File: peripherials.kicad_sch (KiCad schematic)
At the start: 58 parts, among them J11 JST_SH_1x2_SM02B-SRSS-TB-LF-SN, U15 PN7160AHN

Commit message: [#54617] Update bus naming; remove DNP for TVS
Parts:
- D? (x10): DNP DNP -> (none)
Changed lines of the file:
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@@
       (effects (font (size 1.27 1.27) (thickness 0.15)) (justify left bottom) hide)
-    )
-    (property "DNP" "DNP" (at 146.05 213.3599 0)
-      (effects (font (size 1.27 1.27)) (justify left) hide)
     )
     (pin "1")
@@
       (effects (font (size 1.27 1.27) (thickness 0.15)) (justify left bottom) hide)
     )
-    (property "DNP" "DNP" (at 196.85 194.3099 0)
-      (effects (font (size 1.27 1.27)) (justify left) hide)
-    )
     (pin "1")
     (pin "10")
@@
       (effects (font (size 1.27 1.27) (thickness 0.15)) (justify left bottom) hide)
     )
-    (property "DNP" "DNP" (at 146.05 193.0399 0)
-      (effects (font (size 1.27 1.27)) (justify left) hide)
-    )
     (pin "1")
     (pin "10")
@@
       (effects (font (size 1.27 1.27) (thickness 0.15)) (justify left bottom) hide)
     )
-    (property "DNP" "DNP" (at 146.05 173.9899 0)
-      (effects (font (size 1.27 1.27)) (justify left) hide)
-    )
     (pin "1")
     (pin "10")
@@
       (effects (font (size 1.27 1.27) (thickness 0.15)) (justify left bottom) hide)
     )
-    (property "DNP" "DNP" (at 196.85 175.2599 0)
-      (effects (font (size 1.27 1.27)) (justify left) hide)
-    )
     (pin "1")
     (pin "10")
@@
       (effects (font (size 1.27 1.27) (thickness 0.15)) (justify left bottom) hide)
     )
-    (property "DNP" "DNP" (at 196.85 233.6799 0)
-      (effects (font (size 1.27 1.27)) (justify left) hide)
-    )
     (pin "1")
     (pin "10")
@@
     (property "License" "Apache-2.0" (at 157.48 245.11 0)
       (effects (font (size 1.27 1.27) (thickness 0.15)) (justify left bottom) hide)
-    )
-    (property "DNP" "DNP" (at 146.05 232.4099 0)
-      (effects (font (size 1.27 1.27)) (justify left) hide)
     )
     (pin "1")
@@
       (effects (font (size 1.27 1.27) (thickness 0.15)) (justify left bottom) hide)
     )
-    (property "DNP" "DNP" (at 196.85 214.6299 0)
-      (effects (font (size 1.27 1.27)) (justify left) hide)
-    )
     (pin "1")
     (pin "10")
@@
       (effects (font (size 1.27 1.27) (thickness 0.15)) (justify left bottom) hide)
     )
-    (property "DNP" "DNP" (at 135.89 109.2199 0)
-      (effects (font (size 1.27 1.27)) (justify left) hide)
-    )
     (pin "1")
     (pin "10")
@@
       (effects (font (size 1.27 1.27) (thickness 0.15)) (justify left bottom) hide)
     )
-    (property "DNP" "DNP" (at 134.62 46.9899 0)
-      (effects (font (size 1.27 1.27)) (justify left) hide)
-    )
-    (pin "1")
+    (pin "1")

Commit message: [#54617] Review requested changes
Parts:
- L? (x2): footprint antmicro-footprints:L_0603_1608Metric -> antmicro-footprints:

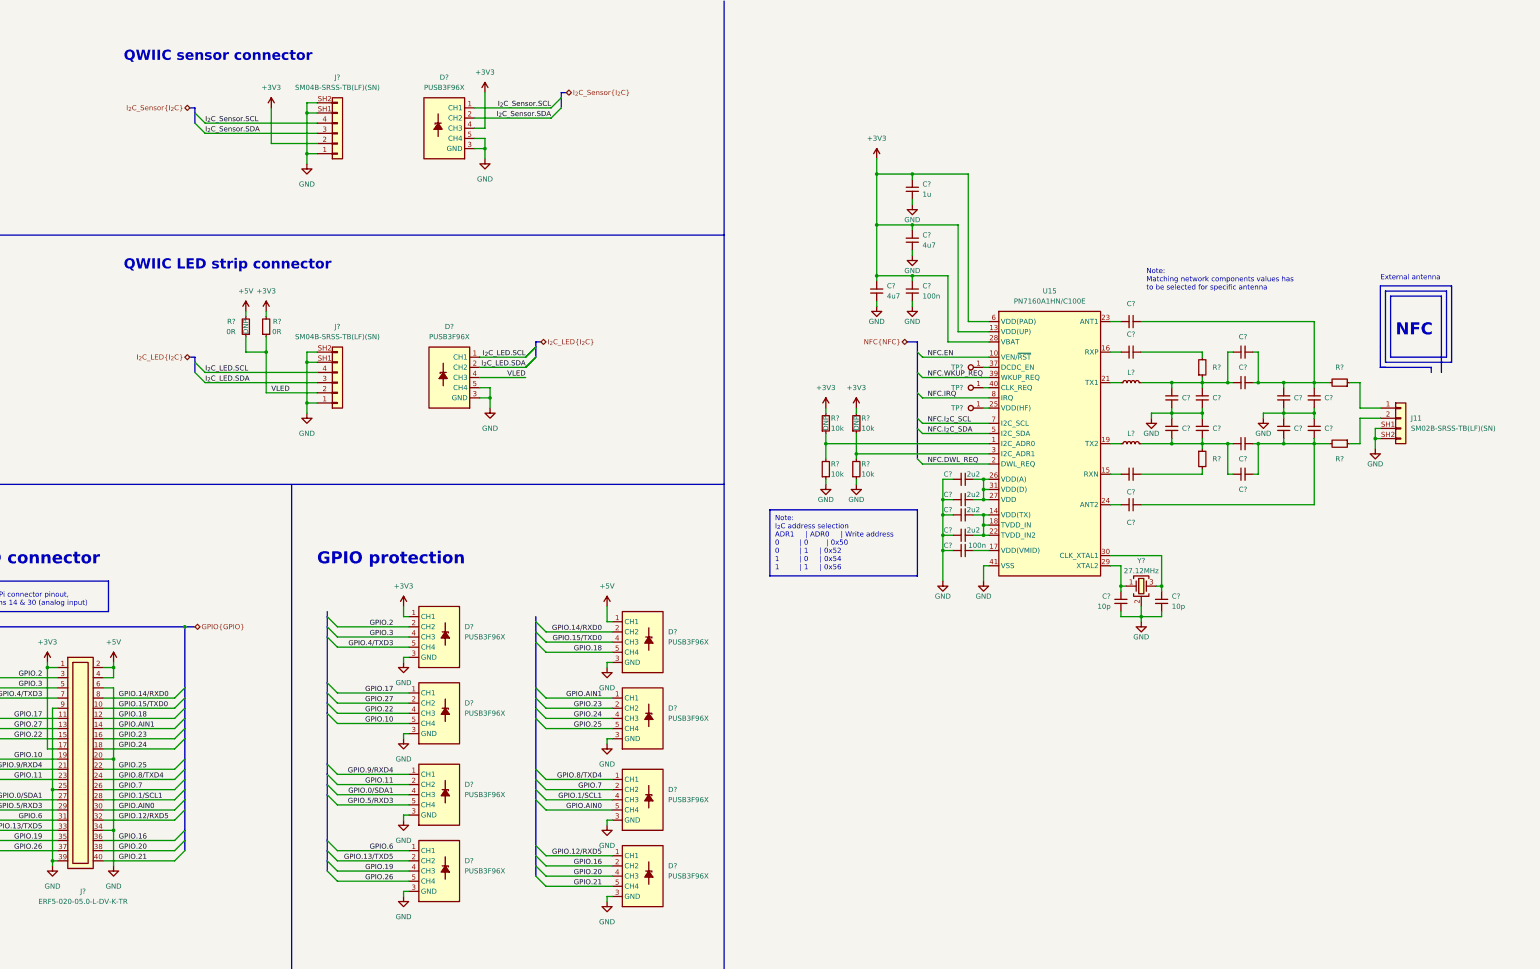
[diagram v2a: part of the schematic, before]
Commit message: [#54617] Re-enumerate reference designators
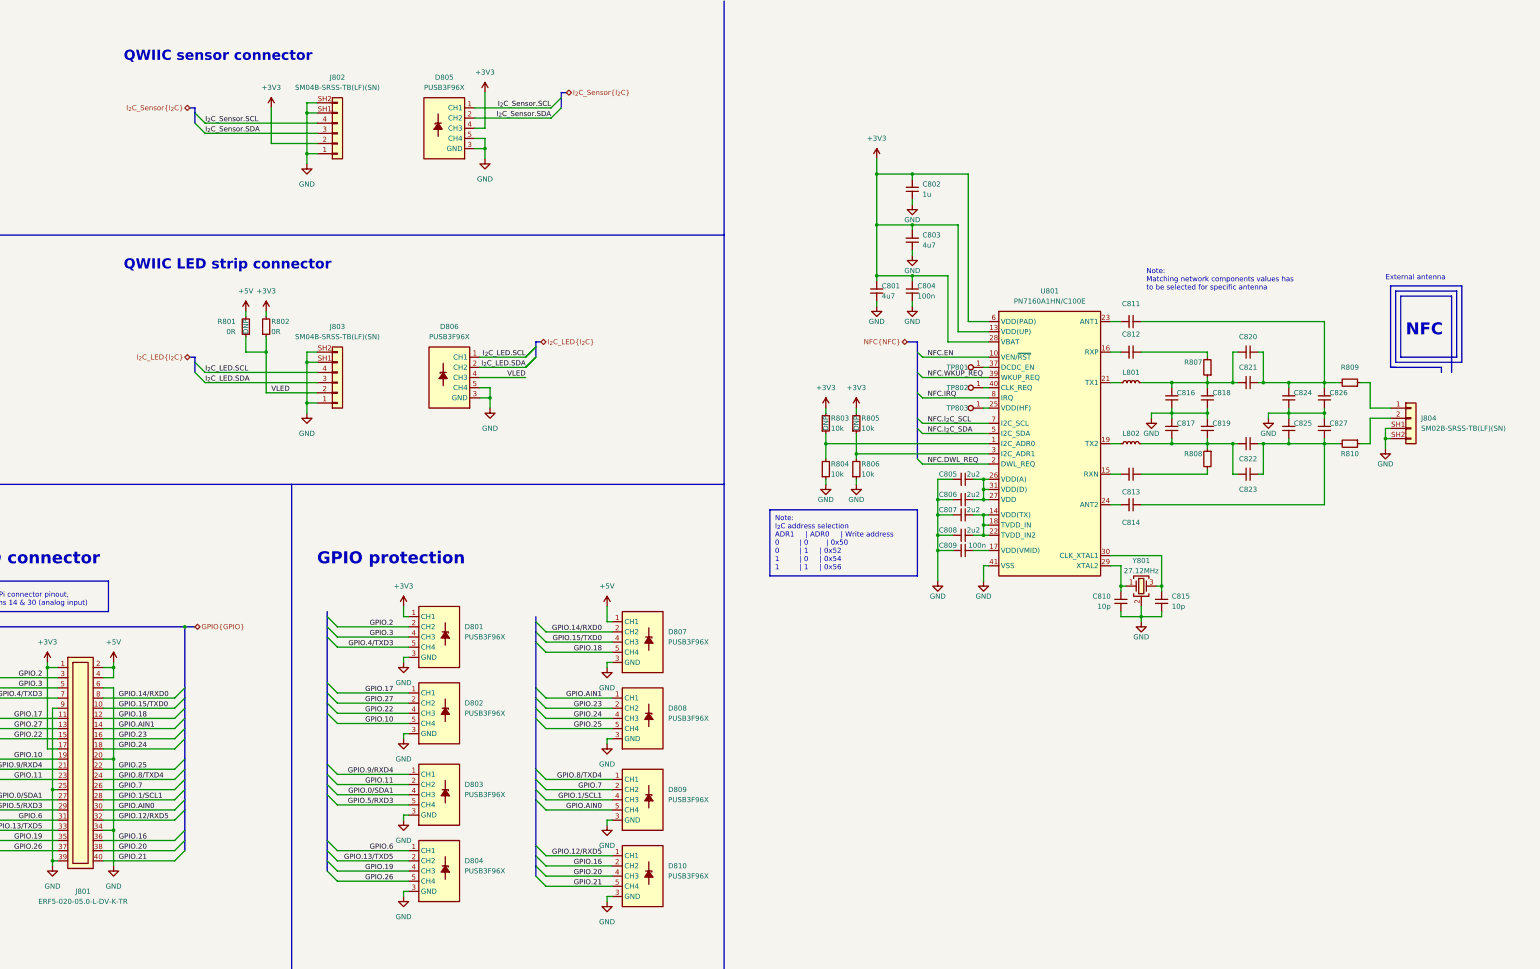
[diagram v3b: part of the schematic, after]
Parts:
- gave numbers to parts that had none: 56
- renumbered J11 to J804, U15 to U801
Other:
- moved on the sheet: C818, C819, C820, C821, C822, C823, C824, C825, C826, C827, J804, R807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

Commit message: [#55181] Rotate board; Change CSI&SD position; Update adapter; NFC placement
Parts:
- L801, L802: footprint antmicro-footprints: -> antmicro-footprints:L_0603_1608Metric
- TP801, TP802, TP803: footprint antmicro-footprints:TP_SMD_1mm -> antmicro-footprints:TP_SMD_0.75mm; symbol antmicroTestPoints:TP_1mm_SMD -> antmicroTestPoints:TP_0.75mm_SMD; now left out of the parts list
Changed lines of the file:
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@@
     )
   )
-  (symbol (lib_id "antmicroTestPoints:TP_1mm_SMD") (at 275.59 114.3 180) (unit 1)
-    (in_bom yes) (on_board yes) (dnp no)
+  (symbol (lib_id "antmicroTestPoints:TP_0.75mm_SMD") (at 275.59 114.3 180) (unit 1)
+    (in_bom no) (on_board yes) (dnp no)
     (property "Reference" "TP803" (at 271.78 114.3 0)
       (effects (font (size 1.27 1.27) (thickness 0.15)) (justify left))
@@
       (effects (font (size 1.27 1.27) (thickness 0.15)) (justify left bottom) hide)
     )
-    (property "Footprint" "antmicro-footprints:TP_SMD_1mm" (at 260.35 104.14 0)
-      (effects (font (size 1.27 1.27) (thickness 0.15)) (justify left bottom) hide)
-    )
-    (property "Datasheet" "" (at 260.35 101.6 0)
-      (effects (font (size 1.27 1.27) (thickness 0.15)) (justify left bottom) hide)
-    )
-    (property "Author" "Antmicro" (at 260.35 99.06 0)
-      (effects (font (size 1.27 1.27) (thickness 0.15)) (justify left bottom) hide)
-    )
-    (property "License" "Apache-2.0" (at 260.35 96.52 0)
-      (effects (font (size 1.27 1.27) (thickness 0.15)) (justify left bottom) hide)
-    )
-    (property "MPN" "" (at 275.59 114.3 0)
-      (effects (font (size 1.27 1.27)) hide)
-    )
-    (property "Manufacturer" "" (at 275.59 114.3 0)
-      (effects (font (size 1.27 1.27)) hide)
+    (property "Footprint" "antmicro-footprints:TP_SMD_0.75mm" (at 264.795 107.95 0)
+      (effects (font (size 1.27 1.27) (thickness 0.15)) (justify left bottom) hide)
+    )
+    (property "Datasheet" "" (at 257.81 101.6 0)
+      (effects (font (size 1.27 1.27) (thickness 0.15)) (justify left bottom) hide)
+    )
+    (property "Author" "Antmicro" (at 264.795 105.41 0)
+      (effects (font (size 1.27 1.27) (thickness 0.15)) (justify left bottom) hide)
+    )
+    (property "License" "Apache-2.0" (at 264.795 102.87 0)
+      (effects (font (size 1.27 1.27) (thickness 0.15)) (justify left bottom) hide)
+    )
+    (property "MPN" "" (at 264.795 102.87 0)
+      (effects (font (size 1.27 1.27) (thickness 0.15)) (justify left bottom) hide)
+    )
+    (property "Manufacturer" "" (at 264.795 107.95 0)
+      (effects (font (size 1.27 1.27) (thickness 0.15)) (justify left bottom) hide)
     )
     (pin "1")
@@
     )
   )
-  (symbol (lib_id "antmicroTestPoints:TP_1mm_SMD") (at 275.59 104.14 180) (unit 1)
-    (in_bom yes) (on_board yes) (dnp no)
+  (symbol (lib_id "antmicroTestPoints:TP_0.75mm_SMD") (at 275.59 104.14 180) (unit 1)
+    (in_bom no) (on_board yes) (dnp no)
     (property "Reference" "TP801" (at 271.78 104.14 0)
       (effects (font (size 1.27 1.27) (thickness 0.15)) (justify left))
@@
       (effects (font (size 1.27 1.27) (thickness 0.15)) (justify left bottom) hide)
     )
-    (property "Footprint" "antmicro-footprints:TP_SMD_1mm" (at 260.35 93.98 0)
-      (effects (font (size 1.27 1.27) (thickness 0.15)) (justify left bottom) hide)
-    )
-    (property "Datasheet" "" (at 260.35 91.44 0)
-      (effects (font (size 1.27 1.27) (thickness 0.15)) (justify left bottom) hide)
-    )
-    (property "Author" "Antmicro" (at 260.35 88.9 0)
-      (effects (font (size 1.27 1.27) (thickness 0.15)) (justify left bottom) hide)
-    )
-    (property "License" "Apache-2.0" (at 260.35 86.36 0)
-      (effects (font (size 1.27 1.27) (thickness 0.15)) (justify left bottom) hide)
-    )
-    (property "MPN" "" (at 275.59 104.14 0)
-      (effects (font (size 1.27 1.27)) hide)
-    )
-    (property "Manufacturer" "" (at 275.59 104.14 0)
-      (effects (font (size 1.27 1.27)) hide)
+    (property "Footprint" "antmicro-footprints:TP_SMD_0.75mm" (at 264.795 97.79 0)
+      (effects (font (size 1.27 1.27) (thickness 0.15)) (justify left bottom) hide)
+    )
+    (property "Datasheet" "" (at 257.81 91.44 0)
+      (effects (font (size 1.27 1.27) (thickness 0.15)) (justify left bottom) hide)
+    )
+    (property "Author" "Antmicro" (at 264.795 95.25 0)
+      (effects (font (size 1.27 1.27) (thickness 0.15)) (justify left bottom) hide)
+    )
+    (property "License" "Apache-2.0" (at 264.795 92.71 0)
+      (effects (font (size 1.27 1.27) (thickness 0.15)) (justify left bottom) hide)
+    )
+    (property "MPN" "" (at 264.795 92.71 0)
+      (effects (font (size 1.27 1.27) (thickness 0.15)) (justify left bottom) hide)
+    )
+    (property "Manufacturer" "" (at 264.795 97.79 0)
+      (effects (font (size 1.27 1.27) (thickness 0.15)) (justify left bottom) hide)
     )
     (pin "1")
@@
       (effects (font (size 1.27 1.27) (thickness 0.15)) (justify left bottom) hide)
     )
-    (property "Footprint" "antmicro-footprints:" (at 323.85 130.81 0)
+    (property "Footprint" "antmicro-footprints:L_0603_1608Metric" (at 323.85 130.81 0)
       (effects (font (size 1.27 1.27) (thickness 0.15)) (justify left bottom) hide)
     )
@@
       (effects (font (size 1.27 1.27) (thickness 0.15)) (justify left bottom) hide)
     )
-    (property "Footprint" "antmicro-footprints:" (at 323.85 115.57 0)
+    (property "Footprint" "antmicro-footprints:L_0603_1608Metric" (at 323.85 115.57 0)
       (effects (font (size 1.27 1.27) (thickness 0.15)) (justify left bottom) hide)
     )
@@
     )
   )
-  (symbol (lib_id "antmicroTestPoints:TP_1mm_SMD") (at 275.59 109.22 180) (unit 1)
-    (in_bom yes) (on_board yes) (dnp no)
+  (symbol (lib_id "antmicroTestPoints:TP_0.75mm_SMD") (at 275.59 109.22 180) (unit 1)
+    (in_bom no) (on_board yes) (dnp no)
     (property "Reference" "TP802" (at 271.78 109.22 0)
       (effects (font (size 1.27 1.27) (thickness 0.15)) (justify left))
@@
       (effects (font (size 1.27 1.27) (thickness 0.15)) (justify left bottom) hide)
     )
-    (property "Footprint" "antmicro-footprints:TP_SMD_1mm" (at 260.35 99.06 0)
-      (effects (font (size 1.27 1.27) (thickness 0.15)) (justify left bottom) hide)
-    )
-    (property "Datasheet" "" (at 260.35 96.52 0)
-      (effects (font (size 1.27 1.27) (thickness 0.15)) (justify left bottom) hide)
-    )
-    (property "Author" "Antmicro" (at 260.35 93.98 0)
-      (effects (font (size 1.27 1.27) (thickness 0.15)) (justify left bottom) hide)
-    )
-    (property "License" "Apache-2.0" (at 260.35 91.44 0)
-      (effects (font (size 1.27 1.27) (thickness 0.15)) (justify left bottom) hide)
-    )
-    (property "MPN" "" (at 275.59 109.22 0)
-      (effects (font (size 1.27 1.27)) hide)
-    )
-    (property "Manufacturer" "" (at 275.59 109.22 0)
-      (effects (font (size 1.27 1.27)) hide)
-    )
-    (pin "1")
+    (property "Footprint" "antmicro-footprints:TP_SMD_0.75mm" (at 264.795 102.87 0)
+      (effects (font (size 1.27 1.27) (thickness 0.15)) (justify left bottom) hide)
+    )
+    (property "Datasheet" "" (at 257.81 96.52 0)
+      (effects (font (size 1.27 1.27) (thickness 0.15)) (justify left bottom) hide)
+    )
+    (property "Author" "Antmicro" (at 264.795 100.33 0)
+      (effects (font (size 1.27 1.27) (thickness 0.15)) (justify left bottom) hide)
+    )
+    (property "License" "Apache-2.0" (at 264.795 97.79 0)
+      (effects (font (size 1.27 1.27) (thickness 0.15)) (justify left bottom) hide)
+    )
+    (property "MPN" "" (at 264.795 97.79 0)
+      (effects (font (size 1.27 1.27) (thickness 0.15)) (justify left bottom) hide)
+    )
+    (property "Manufacturer" "" (at 264.795 102.87 0)
+      (effects (font (size 1.27 1.27) (thickness 0.15)) (justify left bottom) hide)
+    )
+    (pin "1")
